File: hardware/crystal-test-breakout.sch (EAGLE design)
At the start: 11 parts, among them Q1 1N3904

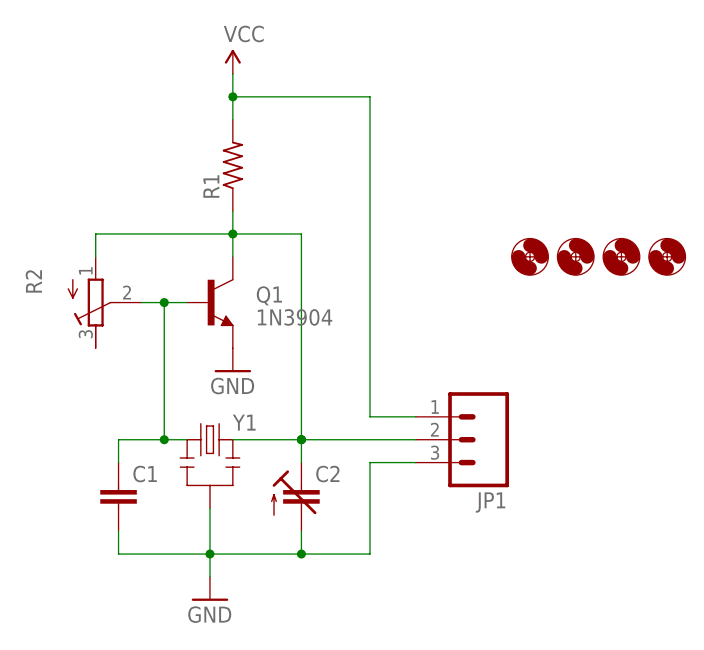
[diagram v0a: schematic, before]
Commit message: putting trimpot on its side for less whoopsy-daisy factor
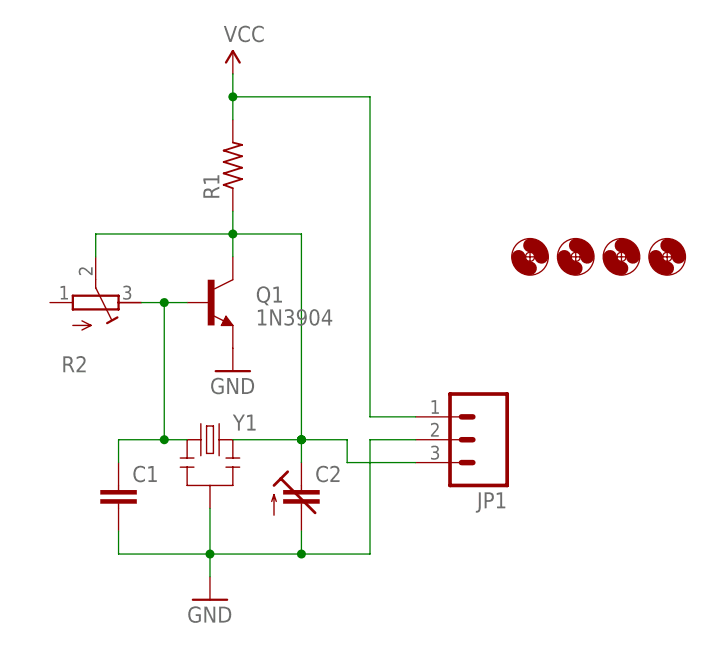
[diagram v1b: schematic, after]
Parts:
- C2: device A_butts:CAPACITOR-TRIMGYC40000 -> A_butts:CAPACITOR-TRIM3050.504
- R2: device A_butts:POTENTIOMETER3296W -> A_butts:POTENTIOMETER3296W-SIDE
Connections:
- net GND: now also JP1.2; no longer JP1.3
- net N$1: now also R2.E; no longer R2.S
- net N$4: now also JP1.3, R2.S; no longer JP1.2, R2.A
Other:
- moved on the sheet: R2
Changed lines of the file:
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@@
 <?xml version="1.0" encoding="utf-8"?>
 <!DOCTYPE eagle SYSTEM "eagle.dtd">
-<eagle version="6.5.0">
+<eagle version="6.4">
 <drawing>
 <settings>
@@
 <setting verticaltext="up"/>
 </settings>
-<grid distance="100" unitdist="mil" unit="mil" style="lines" multiple="1" display="yes" altdistance="1" altunitdist="mil" altunit="mil"/>
+<grid distance="100" unitdist="mil" unit="mil" style="lines" multiple="1" display="yes" altdistance="1" altunitdist="mm" altunit="mm"/>
 <layers>
 <layer number="1" name="Top" color="4" fill="1" visible="yes" active="no"/>
@@
 <part name="R1" library="A_butts" deviceset="RESISTOR" device="PTH-AXIAL-5.08MM"/>
 <part name="Q1" library="A_butts" deviceset="TRANSISTOR_NPN" device="TO-92-AMMO-EBC" value="1N3904"/>
-<part name="C2" library="A_butts" deviceset="CAPACITOR-TRIM" device="GYC40000"/>
-<part name="R2" library="A_butts" deviceset="POTENTIOMETER" device="3296W"/>
+<part name="C2" library="A_butts" deviceset="CAPACITOR-TRIM" device="3050.504"/>
+<part name="R2" library="A_butts" deviceset="POTENTIOMETER" device="3296W-SIDE"/>
 <part name="GND1" library="A_butts" deviceset="GND" device=""/>
 <part name="SUPPLY1" library="A_butts" deviceset="VCC" device=""/>
@@
 <instance part="Q1" gate="G$1" x="60.96" y="73.66"/>
 <instance part="C2" gate="G$1" x="71.12" y="53.34"/>
-<instance part="R2" gate="G$1" x="48.26" y="73.66" rot="MR180"/>
+<instance part="R2" gate="G$1" x="48.26" y="73.66" rot="MR90"/>
 <instance part="GND1" gate="1" x="60.96" y="40.64"/>
 <instance part="SUPPLY1" gate="G$1" x="63.5" y="99.06"/>
@@
 <wire x1="50.8" y1="58.42" x2="55.88" y2="58.42" width="0.1524" layer="91"/>
 <junction x="55.88" y="58.42"/>
-<pinref part="R2" gate="G$1" pin="S"/>
+<pinref part="R2" gate="G$1" pin="E"/>
 <wire x1="53.34" y1="73.66" x2="55.88" y2="73.66" width="0.1524" layer="91"/>
 <junction x="55.88" y="73.66"/>
@@
 <wire x1="71.12" y1="45.72" x2="78.74" y2="45.72" width="0.1524" layer="91"/>
 <junction x="71.12" y="45.72"/>
-<wire x1="78.74" y1="45.72" x2="78.74" y2="55.88" width="0.1524" layer="91"/>
-<pinref part="JP1" gate="G$1" pin="3"/>
-<wire x1="78.74" y1="55.88" x2="83.82" y2="55.88" width="0.1524" layer="91"/>
+<wire x1="78.74" y1="45.72" x2="78.74" y2="58.42" width="0.1524" layer="91"/>
+<pinref part="JP1" gate="G$1" pin="2"/>
+<wire x1="78.74" y1="58.42" x2="83.82" y2="58.42" width="0.1524" layer="91"/>
 </segment>
 </net>
@@
 <wire x1="71.12" y1="81.28" x2="71.12" y2="58.42" width="0.1524" layer="91"/>
 <wire x1="63.5" y1="81.28" x2="48.26" y2="81.28" width="0.1524" layer="91"/>
-<pinref part="JP1" gate="G$1" pin="2"/>
-<wire x1="71.12" y1="58.42" x2="83.82" y2="58.42" width="0.1524" layer="91"/>
 <pinref part="Y1" gate="G$1" pin="3"/>
 <wire x1="63.5" y1="58.42" x2="71.12" y2="58.42" width="0.1524" layer="91"/>
@@
 <junction x="71.12" y="58.42"/>
 <junction x="71.12" y="58.42"/>
-<pinref part="R2" gate="G$1" pin="A"/>
-<wire x1="48.26" y1="81.28" x2="48.26" y2="78.74" width="0.1524" layer="91"/>
-</segment>
-</net>
+<pinref part="R2" gate="G$1" pin="S"/>
+<wire x1="48.26" y1="78.74" x2="48.26" y2="81.28" width="0.1524" layer="91"/>
+<wire x1="71.12" y1="58.42" x2="76.2" y2="58.42" width="0.1524" layer="91"/>
+<wire x1="76.2" y1="58.42" x2="76.2" y2="55.88" width="0.1524" layer="91"/>
+<pinref part="JP1" gate="G$1" pin="3"/>
+<wire x1="76.2" y1="55.88" x2="83.82" y2="55.88" width="0.1524" layer="91"/>
+</segment>
+</net>
